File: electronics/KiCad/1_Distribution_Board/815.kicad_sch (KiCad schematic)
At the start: 47 parts, among them J12 Conn_01x06, J13 Conn_01x10, J14 2.54-1*4P母, J15 2.54-1*4P母, J16 PM254V-11-06-H85, J17 Conn_02x08_Odd_Even, J18 PM254V-11-06-H85, J19 2.54-1*4P母, J20 2.54-1*4P母, U6 PCA9306, U7 PCA9685PW, Y1 25MHz

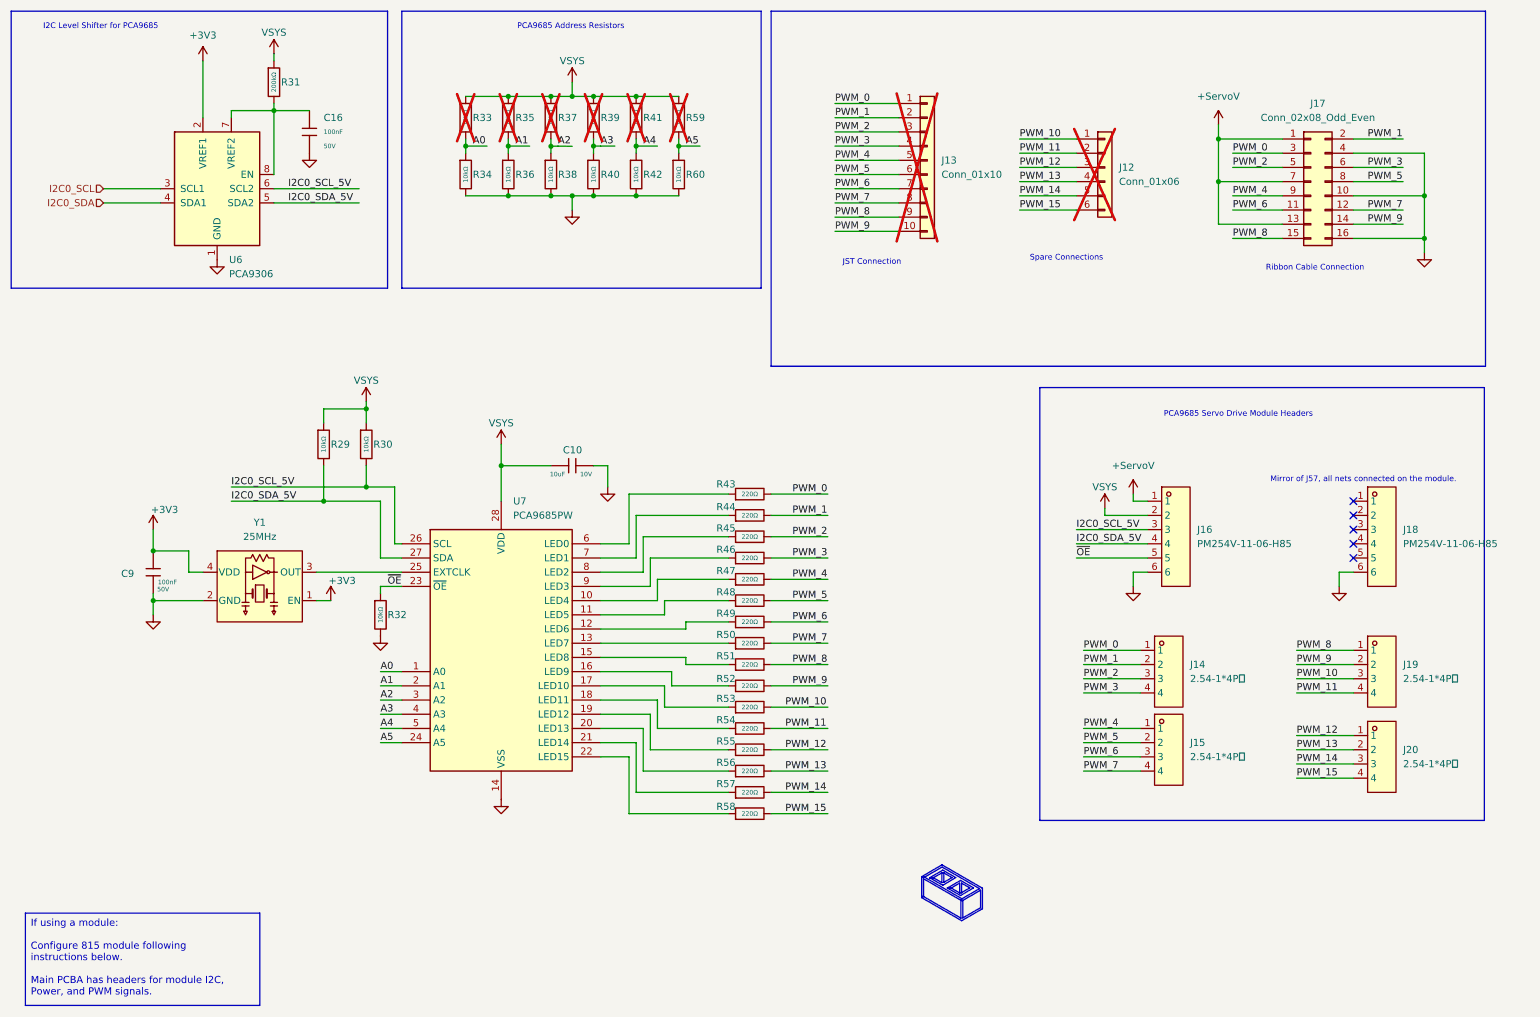
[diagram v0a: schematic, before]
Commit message: Distribution board v1.4.1: effreek's revision, REV label, JLC rotation offsets restored (#1169)
effreek's pull-up/pull-down cleanup and test serial-servo circuit (J11/J14/J15), REV 1.4.1 on the board, the 33 JLC rotation offsets restored, test points out of the position file, and the V1.4.1 Gerber zip. Supersedes #1042.

Co-authored-by: effreek <115494910+effreek@users.noreply.github.com>
Co-Authored-By: Claude Opus 5.5 <noreply@anthropic.com>
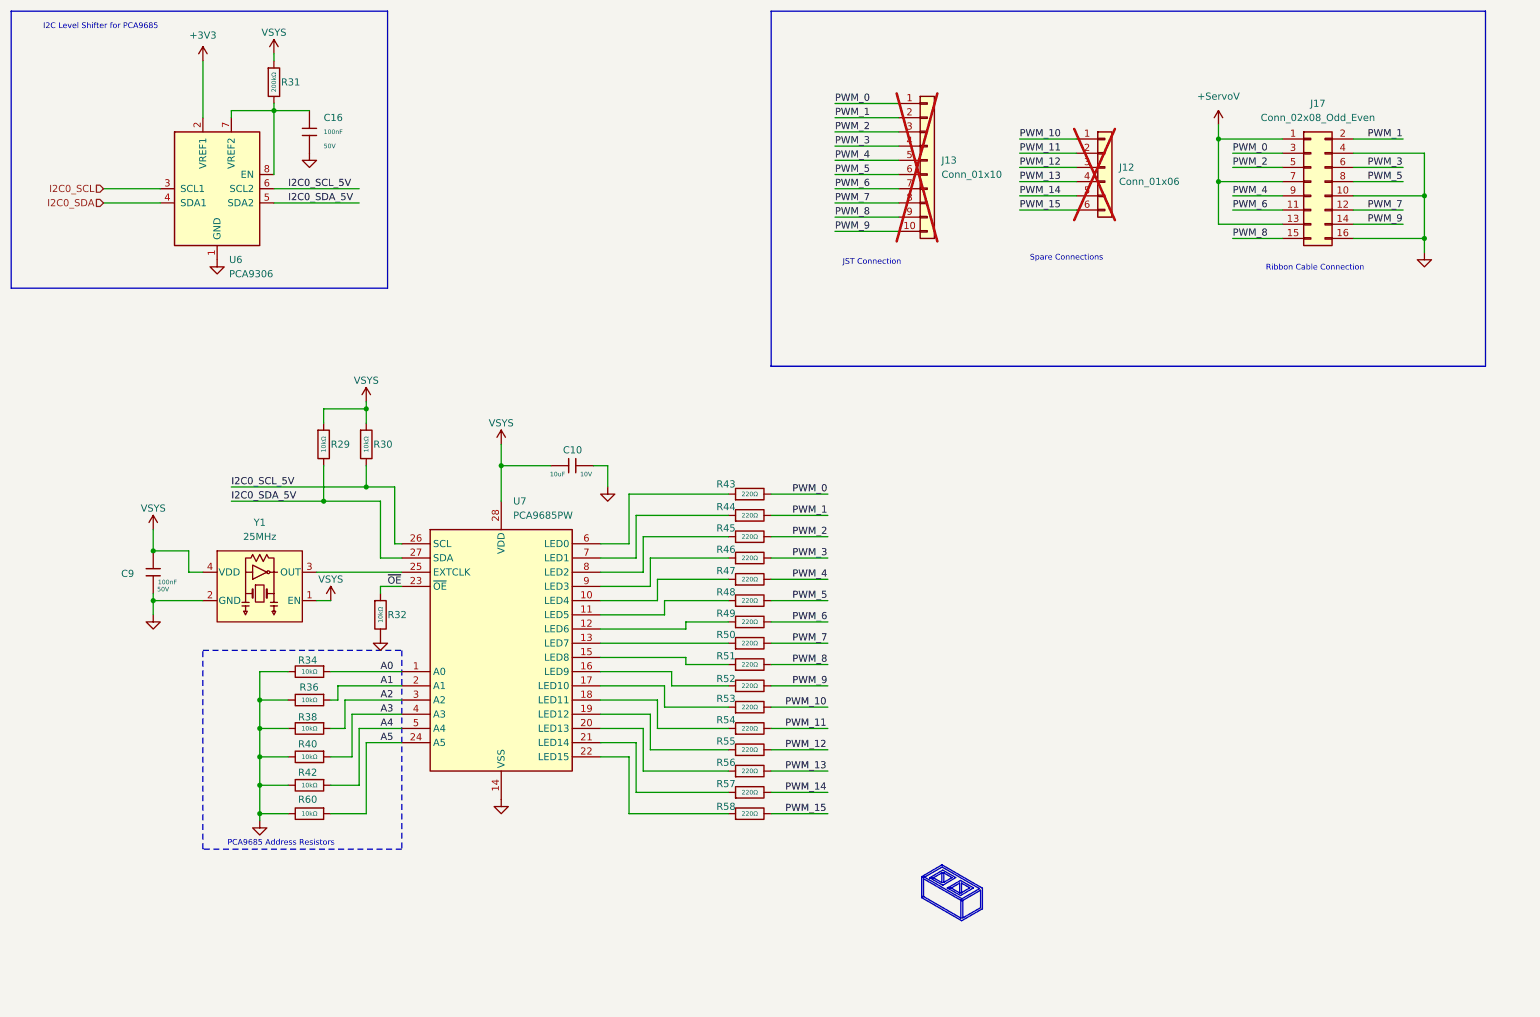
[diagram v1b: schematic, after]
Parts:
- removed J14, J15, J19, J20: 2.54-1*4P母, EasyEDA:HDR-TH_4P-P2.54-V-F, symbol EasyEDA:2.54-1*4P母
- removed J16, J18: PM254V-11-06-H85, EasyEDA:HDR-TH_6P-P2.54-V-F, symbol EasyEDA:PM254V-11-06-H85
- removed R33, R35, R37, R39, R41, R59: 10kΩ, PCM_JLCPCB:R_0603, symbol PCM_JLCPCB-Resistors:0603,10kΩ
- Y1: footprint Crystal_SMD_3.2x2.5mm -> PCM_SparkFun-Clock:Crystal_SMD_3.2x2.5mm; LCSC C669088 -> C41361435; MPN (none) -> SX3M25.000A10F20TNN; Manufacturer (none) -> SCTF; PROD_ID XTAL-25500 -> (none)
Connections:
- net +3V3: no longer C9.2, Y1.1 (EN), Y1.4 (VDD)
- net VSYS: now also C9.2, Y1.1 (EN), Y1.4 (VDD)
- no-connect marks 5 -> 0
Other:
- note removed: "Mirror of J57, all nets connected on the module."
- note removed: "PCA9685 Servo Drive Module Headers"
- moved on the sheet: R34, R36, R38, R40, R42, R60
